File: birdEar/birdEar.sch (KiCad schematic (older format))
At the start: 24 parts, among them J4 Conn_01x02_Male, J6 Conn_01x03_Male, SW2 KSA0A311 LFTR, SW3 KSA0A311 LFTR, U1 LM324, U2 AZ1117EH-3.3TRG1, U4 Si7050-A20, U5 LTR-303ALS-01

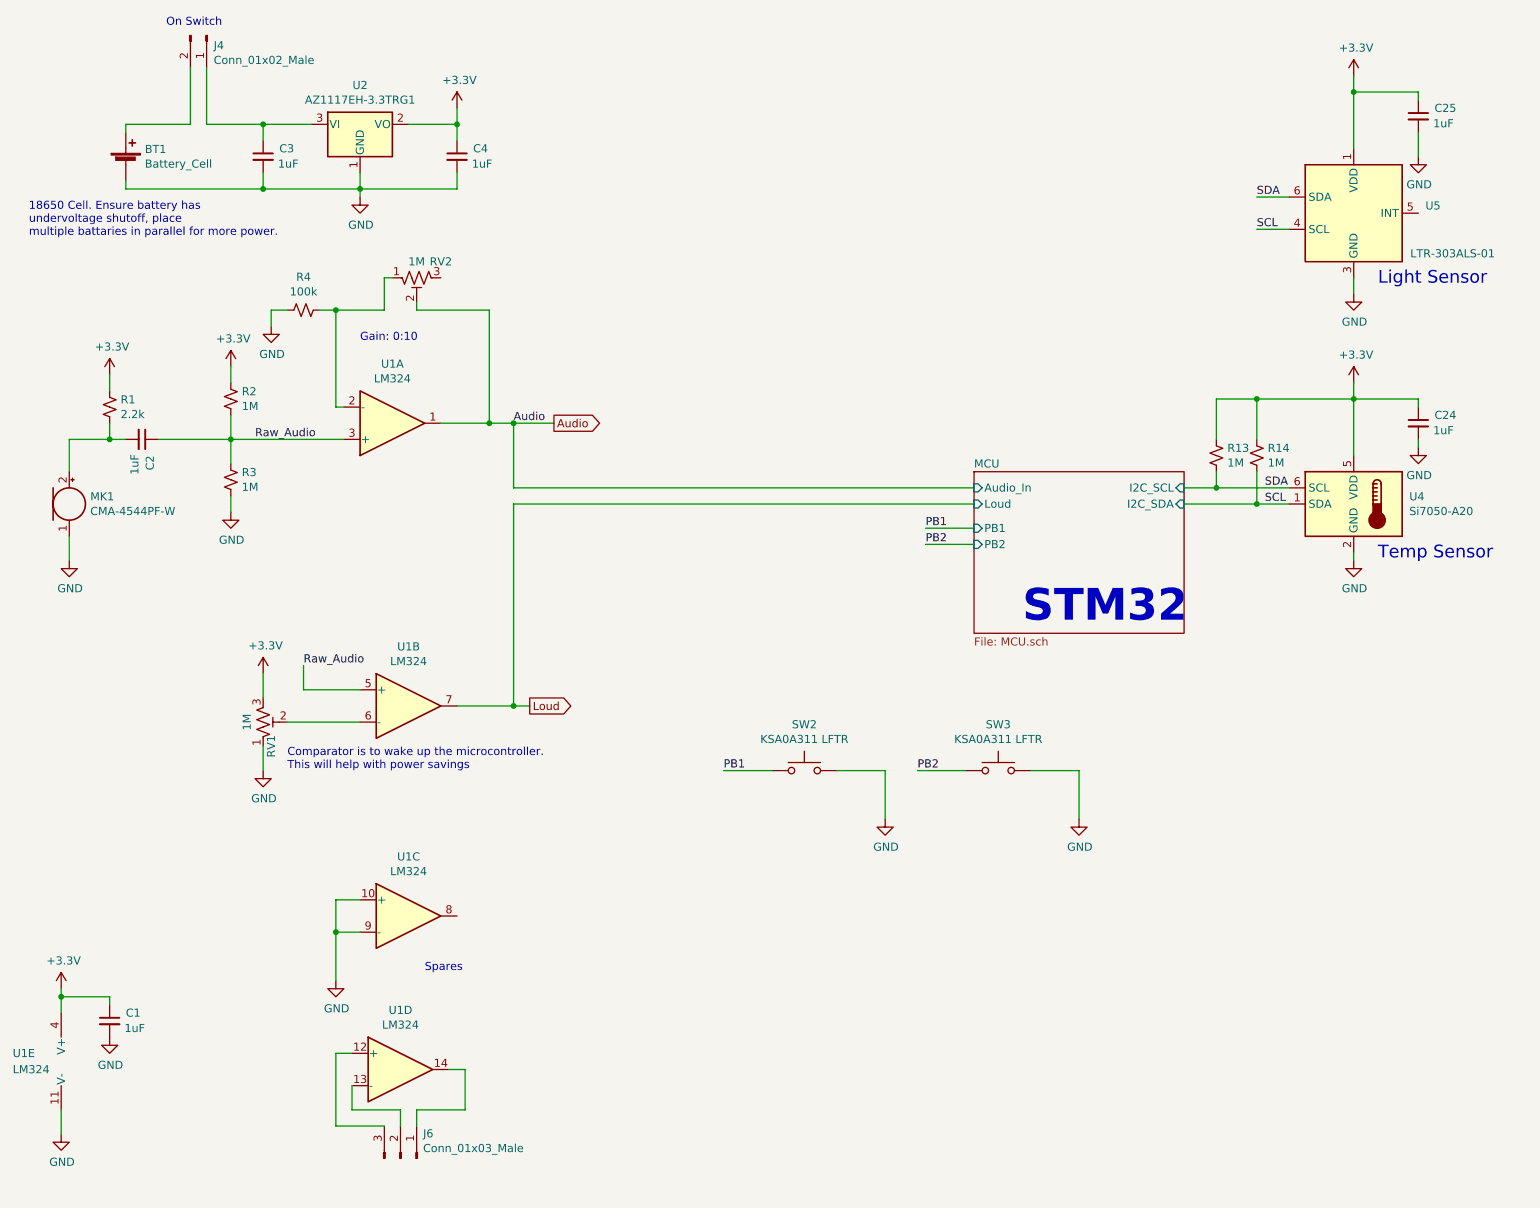
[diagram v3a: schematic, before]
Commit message: Implemented anti aliasing filter, worked on the layout, added some gnd points
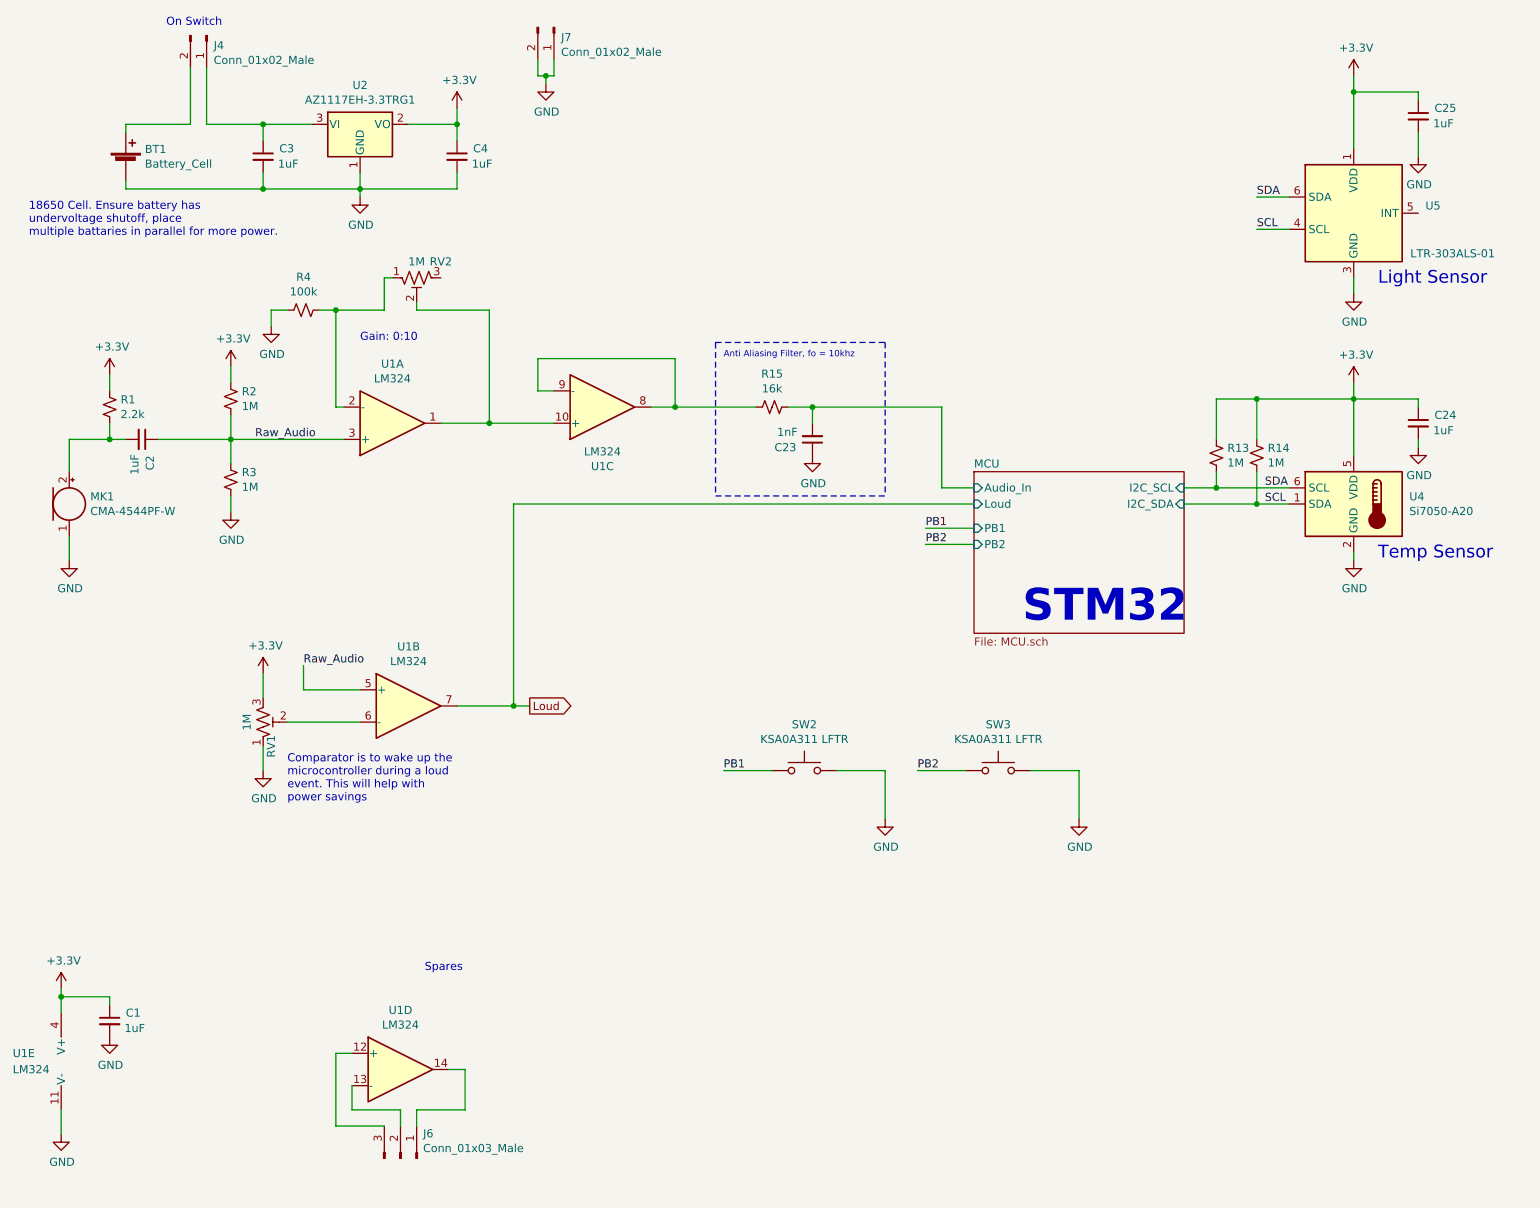
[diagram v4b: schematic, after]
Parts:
- added C23: 1nF, Capacitor_SMD:C_0805_2012Metric, symbol Device:C_Small
- added J7: Conn_01x02_Male, Connector_PinHeader_2.54mm:PinHeader_1x02_P2.54mm_Vertical, symbol Connector:Conn_01x02_Male
- added R15: 16k, Resistor_SMD:R_0805_2012Metric, symbol Device:R_Small_US
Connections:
- net GND: now also C23.1, J7.1 (Pin_1), J7.2 (Pin_2); no longer U1.10 (+), U1.9 (-)
- net at U1.8: now also U1.9 (-), R15.2
- net Audio: no longer names the net of RV2.2, U1.1
- net Audio: now also U1.10 (+)
- new net MCU/Audio_In: C23.2, R15.1
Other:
- note added: "Anti Aliasing Filter, fo = 10khz"
- note added: "Comparator is to wake up the \nmicrocontroller during a loud\nevent. This will help with \npower savings"
- note removed: "Comparator is to wake up the microcontroller.\nThis will help with power savings"
- moved on the sheet: U1C
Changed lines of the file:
@@
 EESchema Schematic File Version 4
 LIBS:birdEar-cache
-EELAYER 26 0
+EELAYER 30 0
 EELAYER END
 $Descr USLetter 11000 8500
@@
 $EndComp
 $Comp
-L power:GND #PWR011
-U 1 1 5D8C40B1
-P 2650 1800
-F 0 "#PWR011" H 2650 1550 50  0001 C CNN
-F 1 "GND" H 2655 1627 50  0000 C CNN
-F 2 "" H 2650 1800 50  0001 C CNN
-F 3 "" H 2650 1800 50  0001 C CNN
-	1    2650 1800
-	1    0    0    -1
-$EndComp
-$Comp
 L Device:C_Small C3
 U 1 1 5D8C4221
@@
 $Comp
 L Amplifier_Operational:LM324 U1
-U 3 1 5D8C5364
-P 2950 6250
-F 0 "U1" H 2950 6617 50  0000 C CNN
-F 1 "LM324" H 2950 6526 50  0000 C CNN
-F 2 "Package_SO:SOIC-14_3.9x8.7mm_P1.27mm" H 2900 6350 50  0001 C CNN
-F 3 "http://www.ti.com/lit/ds/symlink/lm2902-n.pdf" H 3000 6450 50  0001 C CNN
-F 4 "LM324DR" H 2950 6250 50  0001 C CNN "Part Number"
-	3    2950 6250
-	1    0    0    -1
-$EndComp
-$Comp
-L Amplifier_Operational:LM324 U1
 U 4 1 5D8C5409
 P 2900 7200
@@
 Wire Wire Line
 	3450 3200 3150 3200
-Wire Wire Line
-	3450 3200 3600 3200
 Connection ~ 3450 3200
 $Comp
@@
 Text Notes 2650 2700 0    50   ~ 0
 Gain: 0:10
-Text GLabel 3850 3200 2    50   Output ~ 0
-Audio
 Text GLabel 3700 4950 2    50   Output ~ 0
 Loud
@@
 Wire Wire Line
 	2200 5050 2650 5050
-Text Label 3600 3200 0    50   ~ 0
-Audio
 Wire Wire Line
 	2300 4700 2300 4850
@@
 Wire Wire Line
 	3250 4950 3600 4950
-Text Notes 2200 5350 0    50   ~ 0
-Comparator is to wake up the microcontroller.\nThis will help with power savings
 Text Notes 3050 6600 0    50   ~ 0
 Spares
@@
 Wire Wire Line
 	3600 4950 3700 4950
-Wire Wire Line
-	3600 3200 3600 3600
-Wire Wire Line
-	3600 3600 6450 3600
-Connection ~ 3600 3200
-Wire Wire Line
-	3600 3200 3850 3200
 Text Notes 6750 4450 0    197  ~ 39
 STM32
@@
 Wire Wire Line
 	2900 7450 2900 7550
-Wire Wire Line
-	2650 6150 2500 6150
-Wire Wire Line
-	2500 6150 2500 6350
-Wire Wire Line
-	2650 6350 2500 6350
-Connection ~ 2500 6350
-Wire Wire Line
-	2500 6350 2500 6650
-$Comp
-L power:GND #PWR0105
-U 1 1 5DBC4ABE
-P 2500 6650
-F 0 "#PWR0105" H 2500 6400 50  0001 C CNN
-F 1 "GND" H 2505 6477 50  0000 C CNN
-F 2 "" H 2500 6650 50  0001 C CNN
-F 3 "" H 2500 6650 50  0001 C CNN
-	1    2500 6650
-	1    0    0    -1
-$EndComp
+$Comp
+L Connector:Conn_01x02_Male J7
+U 1 1 5D9EC8ED
+P 3850 750
+F 0 "J7" V 3912 794 50  0000 L CNN
+F 1 "Conn_01x02_Male" V 4003 794 50  0000 L CNN
+F 2 "Connector_PinHeader_2.54mm:PinHeader_1x02_P2.54mm_Vertical" H 3850 750 50  0001 C CNN
+F 3 "~" H 3850 750 50  0001 C CNN
+	1    3850 750
+	0    1    1    0
+$EndComp
+Wire Wire Line
+	3750 950  3750 1050
+Wire Wire Line
+	3850 1050 3850 950
+Wire Wire Line
+	3750 1050 3800 1050
+$Comp
+L power:GND #PWR011
+U 1 1 5D8C40B1
+P 2650 1800
+F 0 "#PWR011" H 2650 1550 50  0001 C CNN
+F 1 "GND" H 2655 1627 50  0000 C CNN
+F 2 "" H 2650 1800 50  0001 C CNN
+F 3 "" H 2650 1800 50  0001 C CNN
+	1    2650 1800
+	1    0    0    -1
+$EndComp
+$Comp
+L power:GND #PWR0106
+U 1 1 5D9F52EC
+P 3800 1100
+F 0 "#PWR0106" H 3800 850 50  0001 C CNN
+F 1 "GND" H 3805 927 50  0000 C CNN
+F 2 "" H 3800 1100 50  0001 C CNN
+F 3 "" H 3800 1100 50  0001 C CNN
+	1    3800 1100
+	1    0    0    -1
+$EndComp
+Wire Wire Line
+	3800 1100 3800 1050
+Connection ~ 3800 1050
+Wire Wire Line
+	3800 1050 3850 1050
+Wire Wire Line
+	3450 3200 3850 3200
+$Comp
+L Amplifier_Operational:LM324 U1
+U 3 1 5D8C5364
+P 4150 3100
+F 0 "U1" H 4150 3467 50  0000 C CNN
+F 1 "LM324" H 4150 3376 50  0000 C CNN
+F 2 "Package_SO:SOIC-14_3.9x8.7mm_P1.27mm" H 4100 3200 50  0001 C CNN
+F 3 "http://www.ti.com/lit/ds/symlink/lm2902-n.pdf" H 4200 3300 50  0001 C CNN
+F 4 "LM324DR" H 4150 3100 50  0001 C CNN "Part Number"
+	3    4150 3100
+	1    0    0    1
+$EndComp
+Wire Wire Line
+	3850 3000 3750 3000
+Wire Wire Line
+	3750 3000 3750 2800
+Wire Wire Line
+	3750 2800 4600 2800
+Wire Wire Line
+	4600 2800 4600 3100
+Wire Wire Line
+	4600 3100 4450 3100
+Connection ~ 4600 3100
+$Comp
+L Device:R_Small_US R15
+U 1 1 5DA13BF6
+P 5200 3100
+F 0 "R15" V 4995 3100 50  0000 C CNN
+F 1 "16k" V 5086 3100 50  0000 C CNN
+F 2 "Resistor_SMD:R_0805_2012Metric" H 5200 3100 50  0001 C CNN
+F 3 "~" H 5200 3100 50  0001 C CNN
+	1    5200 3100
+	0    1    1    0
+$EndComp
+$Comp
+L Device:C_Small C23
+U 1 1 5DA147CB
+P 5450 3300
+F 0 "C23" H 5550 3350 50  0000 L CNN
+F 1 "1nF" H 5542 3255 50  0000 L CNN
+F 2 "Capacitor_SMD:C_0805_2012Metric" H 5450 3300 50  0001 C CNN
+F 3 "~" H 5450 3300 50  0001 C CNN
+	1    5450 3300
+	-1   0    0    1
+$EndComp
+Wire Wire Line
+	5300 3100 5450 3100
+Wire Wire Line
+	5450 3100 5450 3200
+Wire Wire Line
+	4600 3100 5100 3100
+Text Notes 4900 2800 0    39   ~ 0
+Anti Aliasing Filter, fo = 10khz
+Wire Notes Line
+	4850 3650 5900 3650
+Wire Notes Line
+	4850 2700 5900 2700
+$Comp
+L power:GND #PWR032
+U 1 1 5DA25816
+P 5450 3400
+F 0 "#PWR032" H 5450 3150 50  0001 C CNN
+F 1 "GND" H 5455 3227 50  0000 C CNN
+F 2 "" H 5450 3400 50  0001 C CNN
+F 3 "" H 5450 3400 50  0001 C CNN
+	1    5450 3400
+	1    0    0    -1
+$EndComp
+Wire Wire Line
+	5450 3100 6250 3100
+Wire Wire Line
+	6250 3100 6250 3600
+Wire Wire Line
+	6250 3600 6450 3600
+Connection ~ 5450 3100
+Wire Notes Line
+	4850 2700 4850 3650
+Wire Notes Line
+	5900 2700 5900 3650
+Text Notes 2200 5550 0    50   ~ 0
+Comparator is to wake up the \nmicrocontroller during a loud\nevent. This will help with \npower savings
 $EndSCHEMATC
